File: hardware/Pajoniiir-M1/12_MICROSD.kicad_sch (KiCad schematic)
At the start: 23 parts

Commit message: hardware: remove stale reset and switched-rail wire stubs
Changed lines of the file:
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@@
   )
   (wire (pts (xy 83.82 47.625) (xy 95.885 47.625)) (stroke (width 0) (type default)))
-  (wire (pts (xy 103.505 47.625) (xy 120.015 47.625)) (stroke (width 0) (type default)))
   (symbol
     (lib_id "Device:C") (at 125.095 51.435 0) (unit 1)

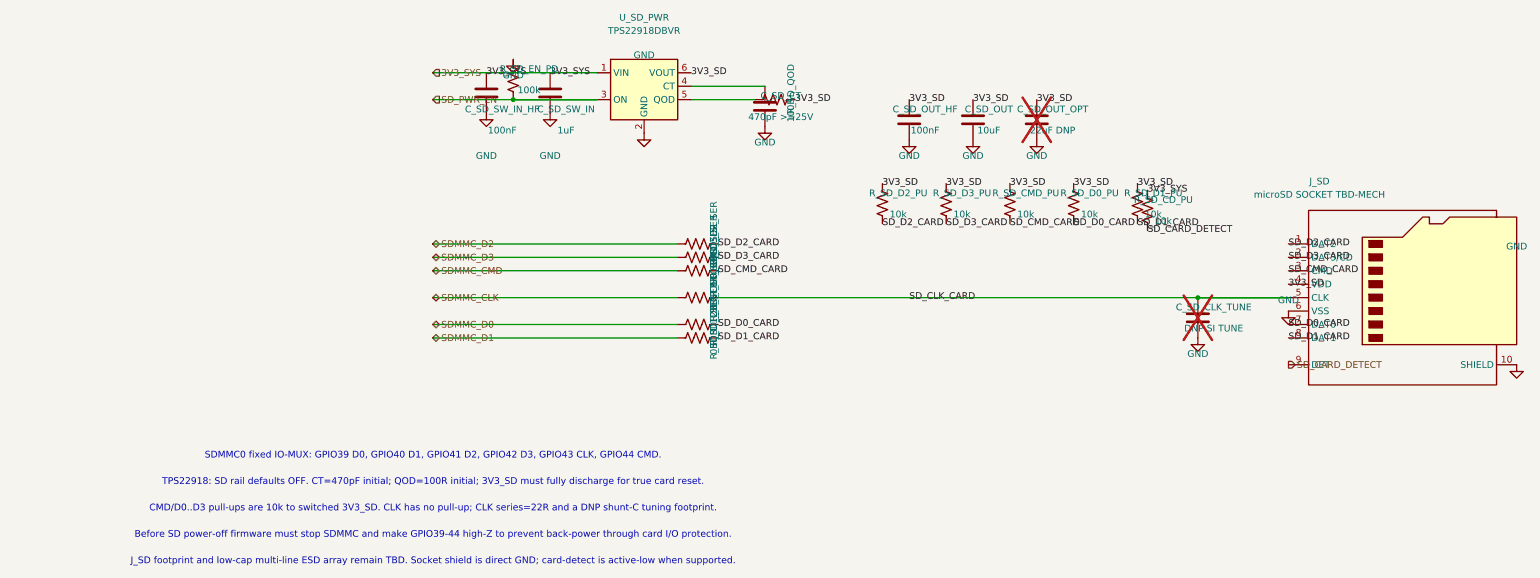
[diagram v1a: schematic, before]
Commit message: hardware: normalize schematic reference designators
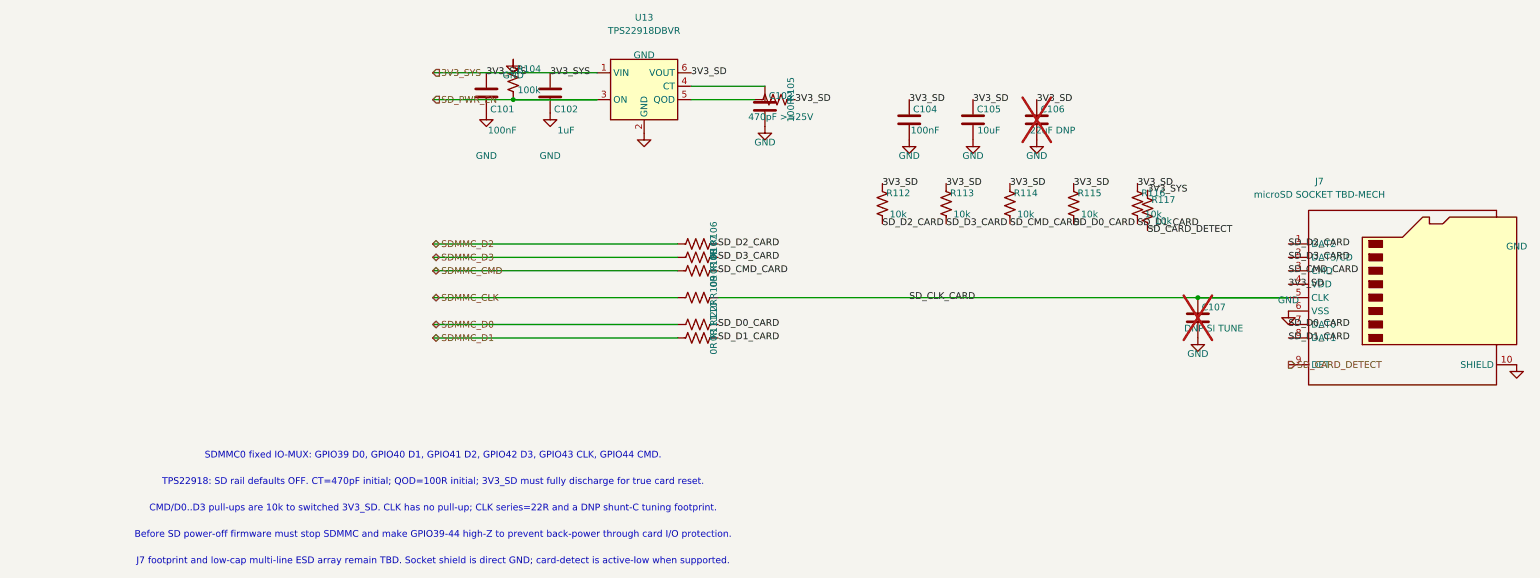
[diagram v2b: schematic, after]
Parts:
- renumbered C_SD_SW_IN_HF to C101, C_SD_SW_IN to C102, C_SD_CT to C103, C_SD_OUT_HF to C104, C_SD_OUT to C105, C_SD_OUT_OPT to C106, C_SD_CLK_TUNE to C107, J_SD to J7, R_SD_EN_PD to R104, R_SD_QOD to R105, R_SD_D2_SER to R106, R_SD_D3_SER to R107, R_SD_CMD_SER to R108, R_SD_CLK_SER to R109, R_SD_D0_SER to R110, R_SD_D1_SER to R111, R_SD_D2_PU to R112, R_SD_D3_PU to R113, R_SD_CMD_PU to R114, R_SD_D0_PU to R115, R_SD_D1_PU to R116, R_SD_CD_PU to R117, U_SD_PWR to U13
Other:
- note added: "J7 footprint and low-cap multi-line ESD array remain TBD. Socket shield is direct GND; card-detect is active-low when supported."
- note removed: "J_SD footprint and low-cap multi-line ESD array remain TBD. Socket shield is direct GND; card-detect is active-low when supported."

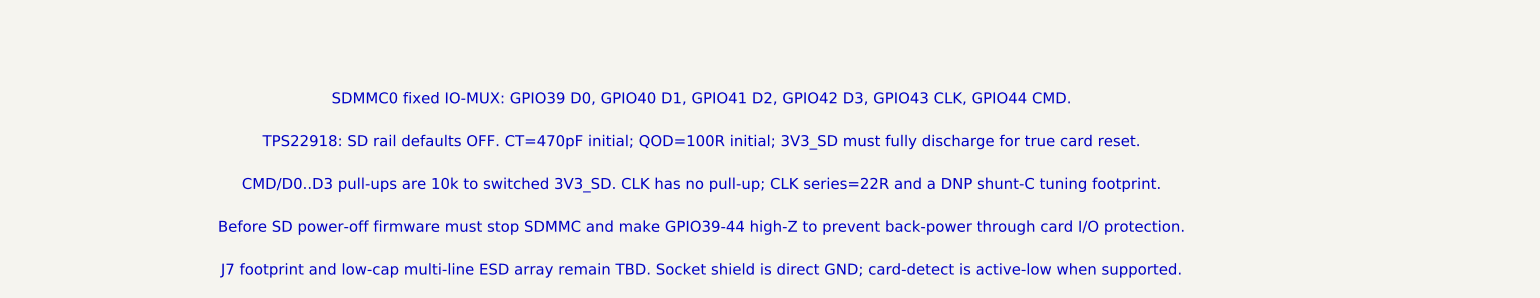
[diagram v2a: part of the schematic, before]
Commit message: hardware: constrain RefDes migration to annotation fields
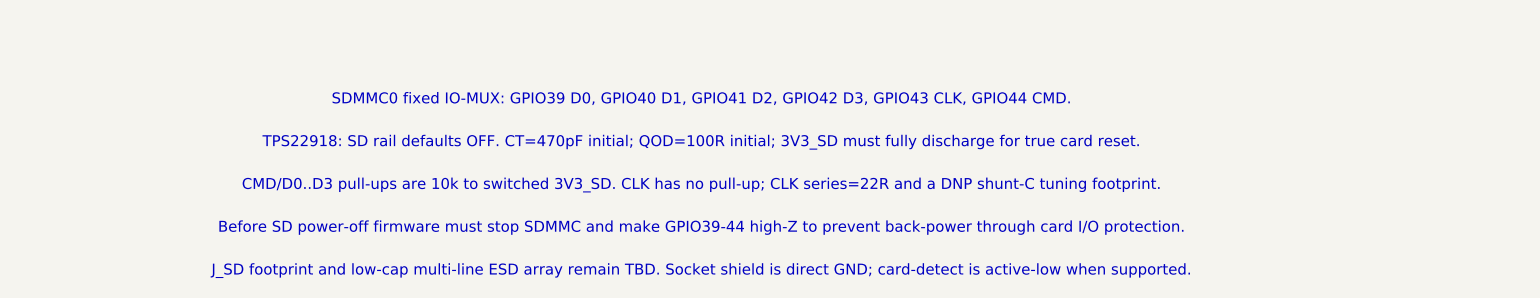
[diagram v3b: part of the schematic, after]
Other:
- note added: "J_SD footprint and low-cap multi-line ESD array remain TBD. Socket shield is direct GND; card-detect is active-low when supported."
- note removed: "J7 footprint and low-cap multi-line ESD array remain TBD. Socket shield is direct GND; card-detect is active-low when supported."
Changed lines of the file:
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@@
   (text "CMD/D0..D3 pull-ups are 10k to switched 3V3_SD. CLK has no pull-up; CLK series=22R and a DNP shunt-C tuning footprint." (exclude_from_sim no) (at 35 125 0) (effects (font (size 1.27 1.27))))
   (text "Before SD power-off firmware must stop SDMMC and make GPIO39-44 high-Z to prevent back-power through card I/O protection." (exclude_from_sim no) (at 35 130 0) (effects (font (size 1.27 1.27))))
-  (text "J7 footprint and low-cap multi-line ESD array remain TBD. Socket shield is direct GND; card-detect is active-low when supported." (exclude_from_sim no) (at 35 135 0) (effects (font (size 1.27 1.27))))
+  (text "J_SD footprint and low-cap multi-line ESD array remain TBD. Socket shield is direct GND; card-detect is active-low when supported." (exclude_from_sim no) (at 35 135 0) (effects (font (size 1.27 1.27))))
   (sheet_instances (path "/" (page "13")))
   (embedded_fonts no)
